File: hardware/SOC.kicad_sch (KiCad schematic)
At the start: 96 parts, among them J1 TF01-A, P1 WF24LTYAJDNN0#, P2 USB-TYPE-C-018, Q1 2N7002K, SW1 K2-1156SP-F5SW-05, SW2 K2-1156SP-F5SW-05, SW3 K2-1156SP-F5SW-05, SW4 K2-1156SP-F5SW-05, SW5 K2-1156SP-F5SW-05, SW6 GT-TC054A-H035-L1, SW7 GT-TC054A-H035-L1, U1 F133, U2 USBLC6-2SC6, U3 MX25L25645GM2I-08G, Y1 12.88727

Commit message: some changes on fab layers
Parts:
- C1, C10, C11, C14, C15, C17, C18, C19, C2, C21, C22, C23, C24, C25, C26, C27, C3: value 100n -> (none); footprint rlib_passive:C_0603_1608Metric -> (none)
- C12, C4, C8: value 10u -> (none); footprint rlib_passive:C_0603_1608Metric -> (none)
- C13: value 1u -> (none); footprint rlib_passive:C_0603_1608Metric -> (none)
- C5, C6: value 18p -> (none); footprint rlib_passive:C_0603_1608Metric -> (none)
- C9: value 2.2u -> (none); footprint rlib_passive:C_0603_1608Metric -> (none)
- D1, D13, D14, D2, D3, D4, D5, D6, D7, D8: value PESD3V3L1BA -> (none); footprint rlib_passive:D_SOD-323F -> (none)
- F1: value 500mA -> (none); footprint rlib_passive:FUSC3216X85N -> (none)
- H1, H2, H3, H4: value MountingHole -> (none); footprint MountingHole:MountingHole_2.5mm_Pad_Via -> (none); symbol Mechanical:MountingHole -> rlib_misc:MountingHole
- J1: value TF01-A -> (none); footprint rlib_connectors:TF-01A -> (none)
- JP1, JP2: value Jumper_2_Open -> (none); footprint Jumper:SolderJumper-2_P1.3mm_Open_TrianglePad1.0x1.5mm -> (none)
- P1: value WF24LTYAJDNN0# -> (none); footprint rlib_lcd:WF24LTYAJDNN0 -> (none)
- P2: value USB-TYPE-C-018 -> (none); footprint rlib_connectors:HRO-TYPE-C-31-M-12 -> (none); LCSC partnumber USB-TYPE-C-018 -> C2765186; Manufacturer DEALON -> SHOU HAN; Mnfct. partnumber DEALON USB-TYPE-C-018 -> TYPE-C 16PIN 2MD(073)
- Q1: value 2N7002K -> (none); footprint rlib_passive:SOT-23 -> (none)
- R1: value 5.1 -> (none); footprint rlib_passive:R_0603_1608Metric -> (none)
- R10, R11, R12, R13, R14, R15, R16, R17, R18, R2, R21, R22, R3, R5, R53, R56, R57, R7, R8, R9: value 10k -> (none); footprint rlib_passive:R_0603_1608Metric -> (none)
- R19, R20, R51, R52: value 27 -> (none); footprint rlib_passive:R_0603_1608Metric -> (none)
- R4, R6: value 100 -> (none); footprint rlib_passive:R_0603_1608Metric -> (none)
- SW1, SW2, SW3, SW4, SW5: value K2-1156SP-F5SW-05 -> (none); footprint rlib_buttons:K2-1156SP-F5SW-05 -> (none)
- SW6, SW7: value GT-TC054A-H035-L1 -> (none); footprint rlib_buttons:GT-TC054A-H035-L1 -> (none)
- TP1: value TestPoint -> (none); footprint TestPoint:TestPoint_Pad_D1.0mm -> (none); now in the parts list
- TP10, TP11, TP12, TP2, TP3, TP4, TP5, TP6, TP7, TP8, TP9: value TestPoint -> (none); footprint TestPoint:TestPoint_Pad_D1.0mm -> (none)
- U1: value F133 -> (none); footprint rlib_ic:LQFP-128_14x14mm_P0.4mm -> (none)
- U2: value USBLC6-2SC6 -> (none); footprint Package_TO_SOT_SMD:SOT-23-6 -> (none)
- U3: value MX25L25645GM2I-08G -> (none); footprint rlib_ic:SOIC-8_5.23x5.23mm_P1.27mm -> (none)
- Y1: value 12.88727 -> (none); footprint rlib_passive:12.88727 -> (none)
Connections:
- net at P2.A6 (D+), U2.4 (I/O2): now also P2.B6 (D+)
- net at P2.A7 (D-), U2.6 (I/O1): now also P2.B7 (D-)
- net LCD_D13: no longer names the net of U1.64 (PD9)
- net LCD_D2: no longer names the net of U1.55 (PD0)
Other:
- moved on the sheet: P2, R57, R8

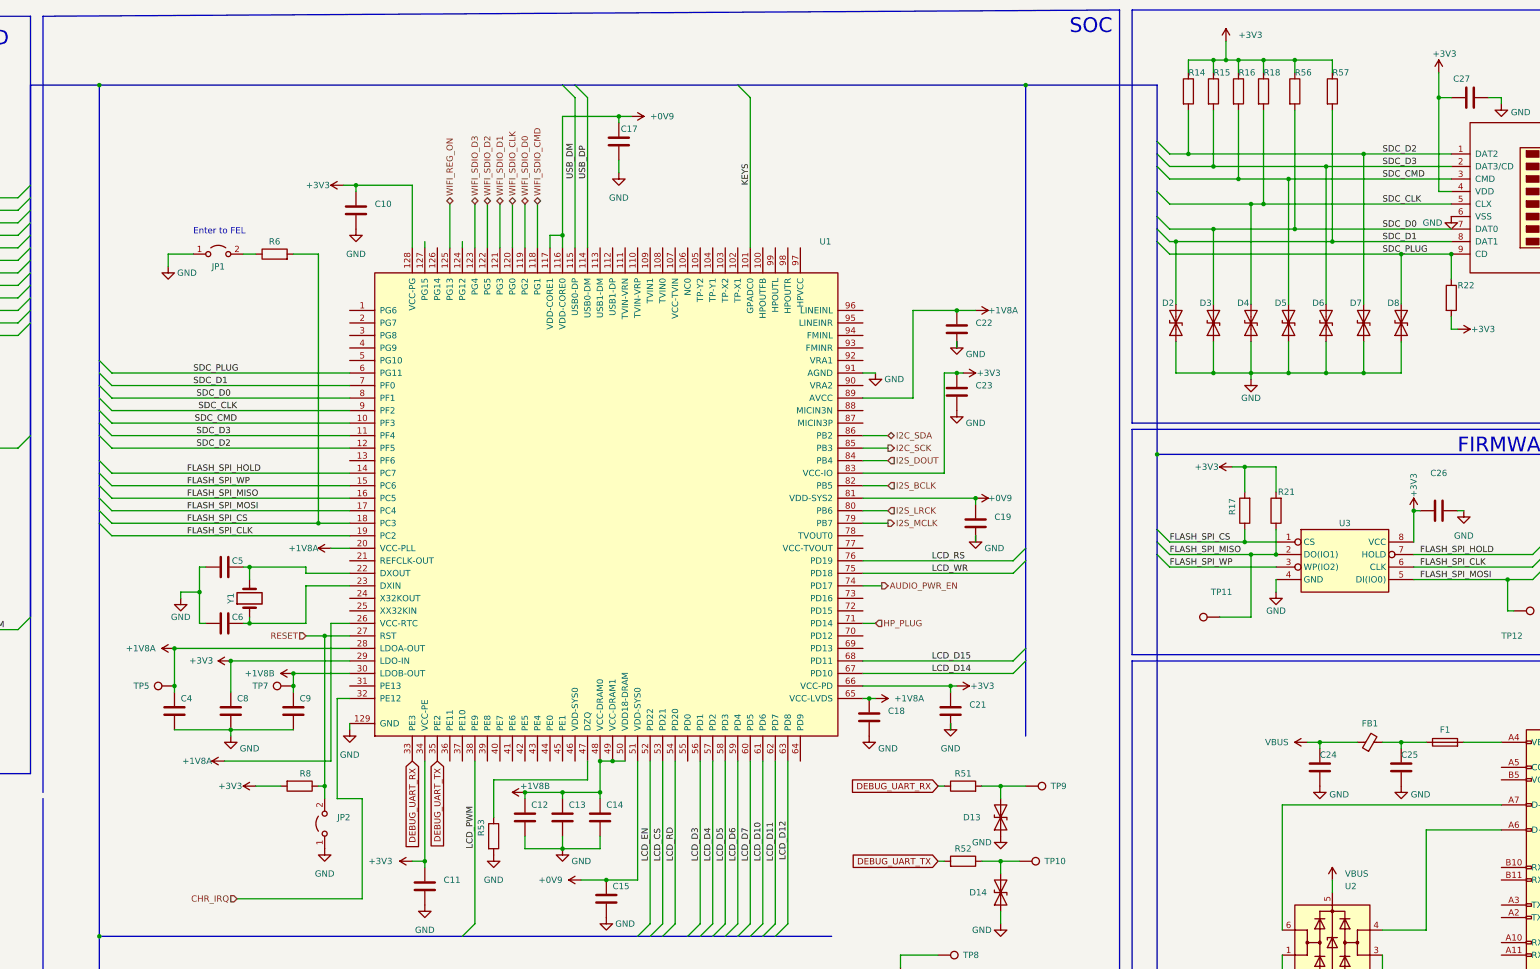
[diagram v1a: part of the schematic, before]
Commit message: pwr btn is optional connected to soc
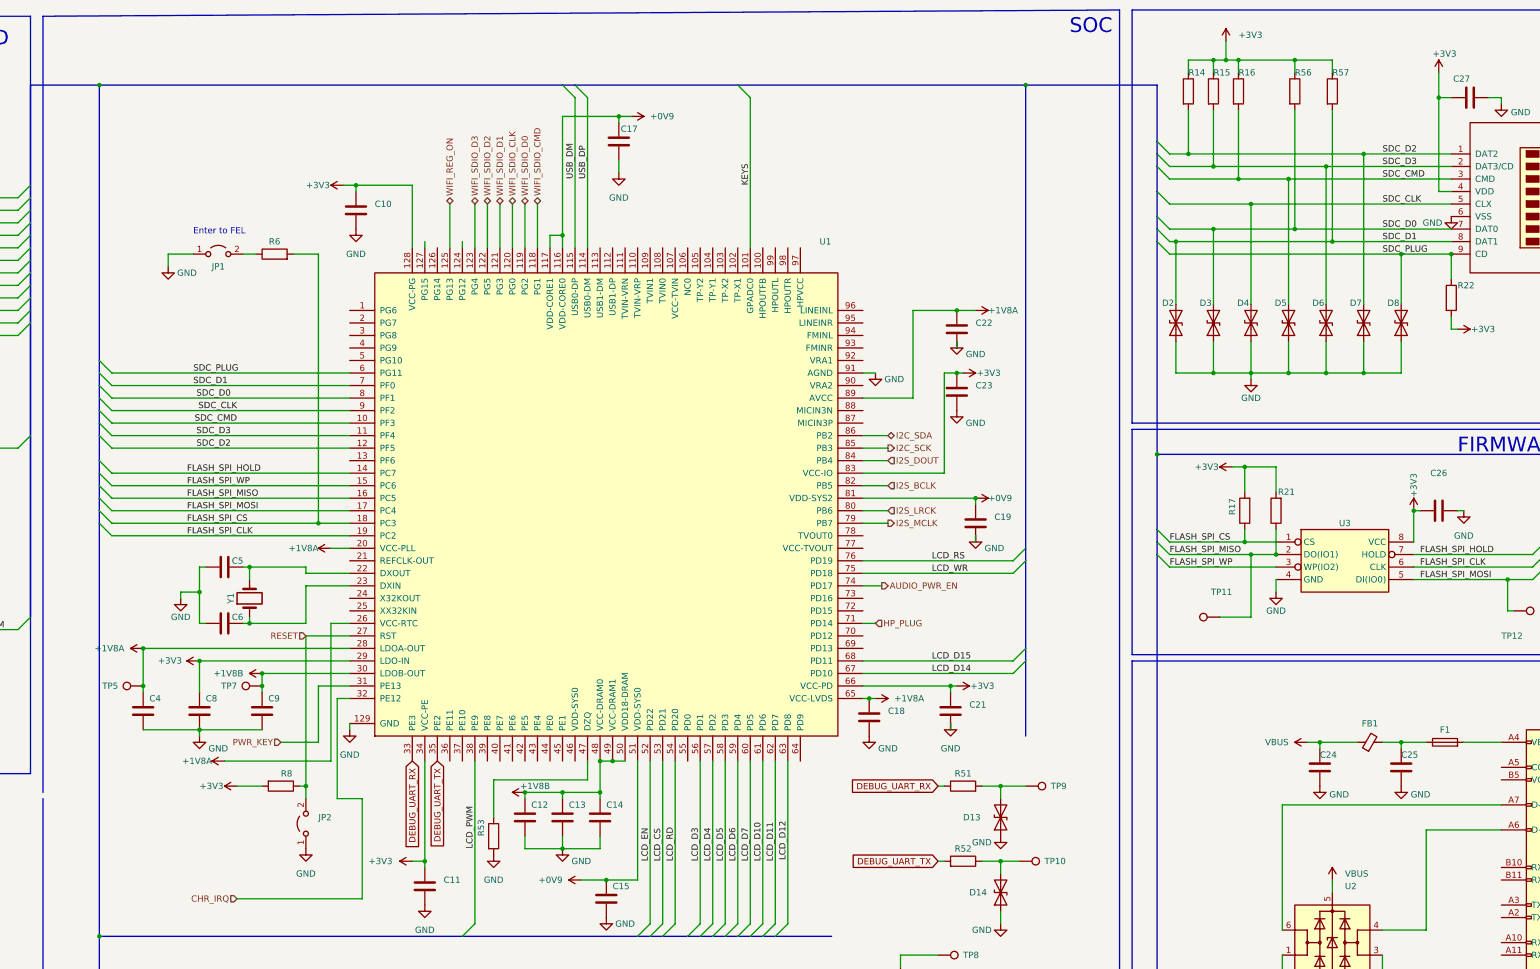
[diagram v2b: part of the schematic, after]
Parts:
- removed R18: (no value), symbol rlib_passive:R
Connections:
- net PWR_KEY: now reaches U1.31 (PE13)
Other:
- moved on the sheet: C4, C8, C9, JP2, R8, TP5, TP7

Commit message: ferrite bead in adc power net is added
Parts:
- added FB1: FerriteBead, rlib_passive:INDC2520X120N, symbol rlib_passive:FerriteBead
- C1, C10, C11, C14, C15, C17, C18, C19, C2, C21, C22, C23, C24, C25, C26, C27, C3: value (none) -> 100n; footprint (none) -> rlib_passive:C_0603_1608Metric
- C12, C4, C8: value (none) -> 10u; footprint (none) -> rlib_passive:C_0603_1608Metric
- C13: value (none) -> 1u; footprint (none) -> rlib_passive:C_0603_1608Metric
- C5, C6: value (none) -> 18p; footprint (none) -> rlib_passive:C_0603_1608Metric
- C9: value (none) -> 2.2u; footprint (none) -> rlib_passive:C_0603_1608Metric
- D1, D13, D14, D2, D3, D4, D5, D6, D7, D8: value (none) -> PESD3V3L1BA; footprint (none) -> rlib_passive:D_SOD-323F
- F1: value (none) -> 500mA; footprint (none) -> rlib_passive:FUSC3216X85N
- H1, H2, H3, H4: value (none) -> MountingHole; footprint (none) -> rlib_misc:MountingHole_2.5mm_Pad_Via
- J1: value (none) -> TF01-A; footprint (none) -> rlib_connectors:TF-01A
- JP1, JP2: value (none) -> Jumper_2_Open; footprint (none) -> Jumper:SolderJumper-2_P1.3mm_Open_TrianglePad1.0x1.5mm
- P1: value (none) -> WF24LTYAJDNN0#; footprint (none) -> rlib_lcd:WF24LTYAJDNN0
- P2: value (none) -> USB-TYPE-C-018; footprint (none) -> rlib_connectors:HRO-TYPE-C-31-M-12
- Q1: value (none) -> 2N7002K; footprint (none) -> rlib_passive:SOT-23
- R1: value (none) -> 5.1; footprint (none) -> rlib_passive:R_0603_1608Metric
- R10, R11, R12, R13, R14, R15, R16, R17, R2, R21, R22, R3, R5, R53, R56, R57, R7, R8, R9: value (none) -> 10k; footprint (none) -> rlib_passive:R_0603_1608Metric
- R19, R20, R51, R52: value (none) -> 27; footprint (none) -> rlib_passive:R_0603_1608Metric
- R4, R6: value (none) -> 100; footprint (none) -> rlib_passive:R_0603_1608Metric
- SW1, SW2, SW3, SW4, SW5: value (none) -> K2-1156SP-F5SW-05; footprint (none) -> rlib_buttons:K2-1156SP-F5SW-05
- SW6, SW7: value (none) -> GT-TC054A-H035-L1; footprint (none) -> rlib_buttons:GT-TC054A-H035-L1
- TP1, TP10, TP11, TP12, TP2, TP3, TP4, TP5, TP6, TP7, TP8, TP9: value (none) -> TestPoint; footprint (none) -> rlib_misc:TestPoint_Pad_D1.0mm
- U1: value (none) -> F133; footprint (none) -> rlib_ic:LQFP-128_14x14mm_P0.4mm
- U2: value (none) -> USBLC6-2SC6; footprint (none) -> Package_TO_SOT_SMD:SOT-23-6
- U3: value (none) -> MX25L25645GM2I-08G; footprint (none) -> rlib_ic:SOIC-8_5.23x5.23mm_P1.27mm
- Y1: value (none) -> 12.88727; footprint (none) -> rlib_passive:12.88727
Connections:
- net +1V8A: now also FB1.2; no longer C22.1, U1.89 (AVCC)
- new net: C22.1, FB1.1, U1.89 (AVCC)
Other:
- moved on the sheet: C22

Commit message: some fixes
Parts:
- U1: value F133 -> (none); footprint rlib_ic:LQFP-128_14x14mm_P0.4mm -> (none)
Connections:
- net USB_DM: now also U1.114 (USB0-DM); no longer U1.115 (USB0-DP)
- net USB_DP: now also U1.115 (USB0-DP); no longer U1.114 (USB0-DM)
- net WIFI_SDIO_D2: now also U1.123 (PG4); no longer U1.122 (PG5)
- net WIFI_SDIO_D3: now also U1.122 (PG5); no longer U1.123 (PG4)
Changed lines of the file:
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@@
     (stroke (width 0) (type default) (color 0 0 0 0))
   )
+  (wire (pts (xy 261.62 85.09) (xy 262.89 85.09))
+    (stroke (width 0) (type default) (color 0 0 0 0))
+  )
   (wire (pts (xy 26.67 57.15) (xy 27.94 57.15))
     (stroke (width 0) (type default) (color 0 0 0 0))
@@
     (effects (font (size 1.27 1.27)) (justify left bottom))
   )
-  (label "USB_DM" (at 179.07 58.42 90)
+  (label "USB_DP" (at 179.07 58.42 90)
     (effects (font (size 1.27 1.27)) (justify left bottom))
   )
@@
     (effects (font (size 1.27 1.27)) (justify left bottom))
   )
-  (label "USB_DP" (at 181.61 58.42 90)
+  (label "USB_DM" (at 181.61 58.42 90)
     (effects (font (size 1.27 1.27)) (justify left bottom))
   )
@@
     (effects (font (size 1.27 1.27)) (justify left))
   )
-  (hierarchical_label "WIFI_SDIO_D2" (shape bidirectional) (at 161.29 63.5 90)
+  (hierarchical_label "WIFI_SDIO_D3" (shape bidirectional) (at 161.29 63.5 90)
     (effects (font (size 1.27 1.27)) (justify left))
   )
@@
     (effects (font (size 1.27 1.27)) (justify left))
   )
-  (hierarchical_label "WIFI_SDIO_D3" (shape bidirectional) (at 158.75 63.5 90)
+  (hierarchical_label "WIFI_SDIO_D2" (shape bidirectional) (at 158.75 63.5 90)
     (effects (font (size 1.27 1.27)) (justify left))
   )
@@
     (in_bom yes) (on_board yes)
     (property "Reference" "U1" (id 0) (at 229.87 71.12 0))
-    (property "Value" "F133" (id 1) (at 231.14 73.66 0))
-    (property "Footprint" "rlib_ic:LQFP-128_14x14mm_P0.4mm" (id 2) (at 232.41 177.8 0)
+    (property "Value" "" (id 1) (at 231.14 73.66 0))
+    (property "Footprint" "" (id 2) (at 232.41 177.8 0)
       (effects (font (size 1.27 1.27)) hide)
     )
-    (property "Datasheet" "DOCUMENTATION" (id 3) (at 234.95 175.26 0)
+    (property "Datasheet" "${RLIB}/ic/datasheets/D1S.pdf" (id 3) (at 234.95 175.26 0)
       (effects (font (size 1.27 1.27)) hide)
     )
@@
     (in_bom yes) (on_board yes)
     (property "Reference" "FB1" (id 0) (at 340.36 168.91 90))
-    (property "Value" "" (id 1) (at 340.3219 168.91 90)
+    (property "Value" "FerriteBead" (id 1) (at 340.3219 168.91 90)
       (effects (font (size 1.27 1.27)) hide)
     )
-    (property "Footprint" "" (id 2) (at 340.36 174.498 90)
+    (property "Footprint" "rlib_passive:C_0805_2012Metric" (id 2) (at 340.36 174.498 90)
       (effects (font (size 1.27 1.27)) hide)
     )
@@
     (pin "2")
   )
-  (symbol (lib_name "+1V8A_4") (lib_id "rlib_power:+1V8A") (at 262.89 85.09 270) (unit 1)
+  (symbol (lib_name "+1V8A_4") (lib_id "rlib_power:+1V8A") (at 261.62 85.09 270) (unit 1)
     (in_bom yes) (on_board yes)
-    (property "Reference" "#PWR0131" (id 0) (at 259.08 85.09 0)
+    (property "Reference" "#PWR0131" (id 0) (at 257.81 85.09 0)
       (effects (font (size 1.27 1.27)) hide)
     )
-    (property "Value" "+1V8A" (id 1) (at 265.43 85.09 90)
+    (property "Value" "+1V8A" (id 1) (at 264.16 85.09 90)
       (effects (font (size 1.27 1.27)) (justify left))
     )
-    (property "Footprint" "" (id 2) (at 262.89 85.09 0)
+    (property "Footprint" "" (id 2) (at 261.62 85.09 0)
       (effects (font (size 1.27 1.27)) hide)
     )
-    (property "Datasheet" "" (id 3) (at 262.89 85.09 0)
+    (property "Datasheet" "" (id 3) (at 261.62 85.09 0)
       (effects (font (size 1.27 1.27)) hide)
     )
@@
     (in_bom yes) (on_board yes)
     (property "Reference" "FB4" (id 0) (at 260.35 81.28 90))
-    (property "Value" "" (id 1) (at 260.3119 81.28 90)
+    (property "Value" "FerriteBead" (id 1) (at 260.3119 81.28 90)
       (effects (font (size 1.27 1.27)) hide)
     )
-    (property "Footprint" "" (id 2) (at 260.35 86.868 90)
+    (property "Footprint" "rlib_passive:C_0805_2012Metric" (id 2) (at 260.35 86.868 90)
       (effects (font (size 1.27 1.27)) hide)
     )

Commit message: xxx
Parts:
- removed TP7: TestPoint, rlib_misc:TestPoint_Pad_D1.0mm, symbol Connector:TestPoint
- R6: value 100 -> 50
- U1: value (none) -> F133; footprint (none) -> rlib_ic:LQFP-128_14x14mm_P0.4mm
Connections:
- net +1V8A: now also R5.1
- net +3V3: no longer R5.1
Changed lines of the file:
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@@
   (junction (at 96.52 246.38) (diameter 0) (color 0 0 0 0)
   )
-  (junction (at 115.57 161.29) (diameter 0) (color 0 0 0 0)
-  )
   (junction (at 331.47 55.88) (diameter 0) (color 0 0 0 0)
   )
@@
     (stroke (width 0) (type default) (color 0 0 0 0))
   )
-  (wire (pts (xy 115.57 158.75) (xy 115.57 161.29))
+  (wire (pts (xy 115.57 158.75) (xy 115.57 162.56))
     (stroke (width 0) (type default) (color 0 0 0 0))
   )
@@
     (stroke (width 0) (type default) (color 0 0 0 0))
   )
-  (wire (pts (xy 46.99 123.19) (xy 46.99 128.27))
+  (wire (pts (xy 46.99 123.19) (xy 46.99 125.73))
     (stroke (width 0) (type default) (color 0 0 0 0))
   )
@@
     (stroke (width 0) (type default) (color 0 0 0 0))
   )
+  (wire (pts (xy 120.65 237.49) (xy 120.65 238.76))
+    (stroke (width 0) (type default) (color 0 0 0 0))
+  )
   (wire (pts (xy 99.06 143.51) (xy 99.06 142.24))
     (stroke (width 0) (type default) (color 0 0 0 0))
@@
     (stroke (width 0) (type default) (color 0 0 0 0))
   )
-  (wire (pts (xy 115.57 161.29) (xy 115.57 162.56))
-    (stroke (width 0) (type default) (color 0 0 0 0))
-  )
   (wire (pts (xy 26.67 77.47) (xy 66.04 77.47))
     (stroke (width 0) (type default) (color 0 0 0 0))
@@
     (in_bom yes) (on_board yes)
     (property "Reference" "U1" (id 0) (at 229.87 71.12 0))
-    (property "Value" "" (id 1) (at 231.14 73.66 0))
-    (property "Footprint" "" (id 2) (at 232.41 177.8 0)
+    (property "Value" "F133" (id 1) (at 231.14 73.66 0))
+    (property "Footprint" "rlib_ic:LQFP-128_14x14mm_P0.4mm" (id 2) (at 232.41 177.8 0)
       (effects (font (size 1.27 1.27)) hide)
     )
@@
     (pin "1")
   )
+  (symbol (lib_name "+1V8A_4") (lib_id "rlib_power:+1V8A") (at 120.65 237.49 0) (unit 1)
+    (in_bom yes) (on_board yes)
+    (property "Reference" "#PWR0143" (id 0) (at 120.65 241.3 0)
+      (effects (font (size 1.27 1.27)) hide)
+    )
+    (property "Value" "+1V8A" (id 1) (at 116.84 233.68 0)
+      (effects (font (size 1.27 1.27)) (justify left))
+    )
+    (property "Footprint" "" (id 2) (at 120.65 237.49 0)
+      (effects (font (size 1.27 1.27)) hide)
+    )
+    (property "Datasheet" "" (id 3) (at 120.65 237.49 0)
+      (effects (font (size 1.27 1.27)) hide)
+    )
+    (pin "1")
+  )
   (symbol (lib_id "Jumper:Jumper_2_Open") (at 124.46 189.23 90) (unit 1)
     (in_bom no) (on_board yes)
@@
     (pin "1")
   )
-  (symbol (lib_id "Connector:TestPoint") (at 115.57 161.29 90) (unit 1)
-    (in_bom yes) (on_board yes)
-    (property "Reference" "TP7" (id 0) (at 110.49 161.29 90)
-      (effects (font (size 1.27 1.27)) (justify left))
-    )
-    (property "Value" "TestPoint" (id 1) (at 116.84 162.56 90)
-      (effects (font (size 1.27 1.27)) (justify left) hide)
-    )
-    (property "Footprint" "rlib_misc:TestPoint_Pad_D1.0mm" (id 2) (at 115.57 156.21 0)
-      (effects (font (size 1.27 1.27)) hide)
-    )
-    (property "Datasheet" "~" (id 3) (at 115.57 156.21 0)
-      (effects (font (size 1.27 1.27)) hide)
-    )
-    (pin "1")
-  )
   (symbol (lib_id "rlib_passive:R") (at 228.6 246.38 90) (unit 1)
     (in_bom yes) (on_board yes)
@@
     (in_bom yes) (on_board yes)
     (property "Reference" "R6" (id 0) (at 118.11 71.12 90))
-    (property "Value" "100" (id 1) (at 118.11 76.2 90))
+    (property "Value" "50" (id 1) (at 118.11 76.2 90))
     (property "Footprint" "rlib_passive:R_0603_1608Metric" (id 2) (at 118.11 75.438 90)
       (effects (font (size 1.27 1.27)) hide)
@@
     (pin "1")
   )
-  (symbol (lib_id "power:+3V3") (at 46.99 128.27 270) (unit 1)
+  (symbol (lib_id "power:+3V3") (at 46.99 125.73 270) (unit 1)
     (in_bom yes) (on_board yes) (fields_autoplaced)
-    (property "Reference" "#PWR07" (id 0) (at 43.18 128.27 0)
+    (property "Reference" "#PWR07" (id 0) (at 43.18 125.73 0)
       (effects (font (size 1.27 1.27)) hide)
     )
-    (property "Value" "+3V3" (id 1) (at 50.8 128.2699 90)
+    (property "Value" "+3V3" (id 1) (at 50.8 125.7299 90)
       (effects (font (size 1.27 1.27)) (justify left))
     )
-    (property "Footprint" "" (id 2) (at 46.99 128.27 0)
+    (property "Footprint" "" (id 2) (at 46.99 125.73 0)
       (effects (font (size 1.27 1.27)) hide)
     )
-    (property "Datasheet" "" (id 3) (at 46.99 128.27 0)
+    (property "Datasheet" "" (id 3) (at 46.99 125.73 0)
       (effects (font (size 1.27 1.27)) hide)
     )
@@
       (effects (font (size 1.27 1.27)) hide)
     )
-    (pin "1")
-  )
-  (symbol (lib_id "power:+3V3") (at 120.65 238.76 0) (unit 1)
-    (in_bom yes) (on_board yes)
-    (property "Reference" "#PWR017" (id 0) (at 120.65 242.57 0)
-      (effects (font (size 1.27 1.27)) hide)
-    )
-    (property "Value" "+3V3" (id 1) (at 118.11 234.95 0)
-      (effects (font (size 1.27 1.27)) (justify left))
-    )
-    (property "Footprint" "" (id 2) (at 120.65 238.76 0)
-      (effects (font (size 1.27 1.27)) hide)
-    )
-    (property "Datasheet" "" (id 3) (at 120.65 238.76 0)
-      (effects (font (size 1.27 1.27)) hide)
-    )
